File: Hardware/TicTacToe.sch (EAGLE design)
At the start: 42 parts

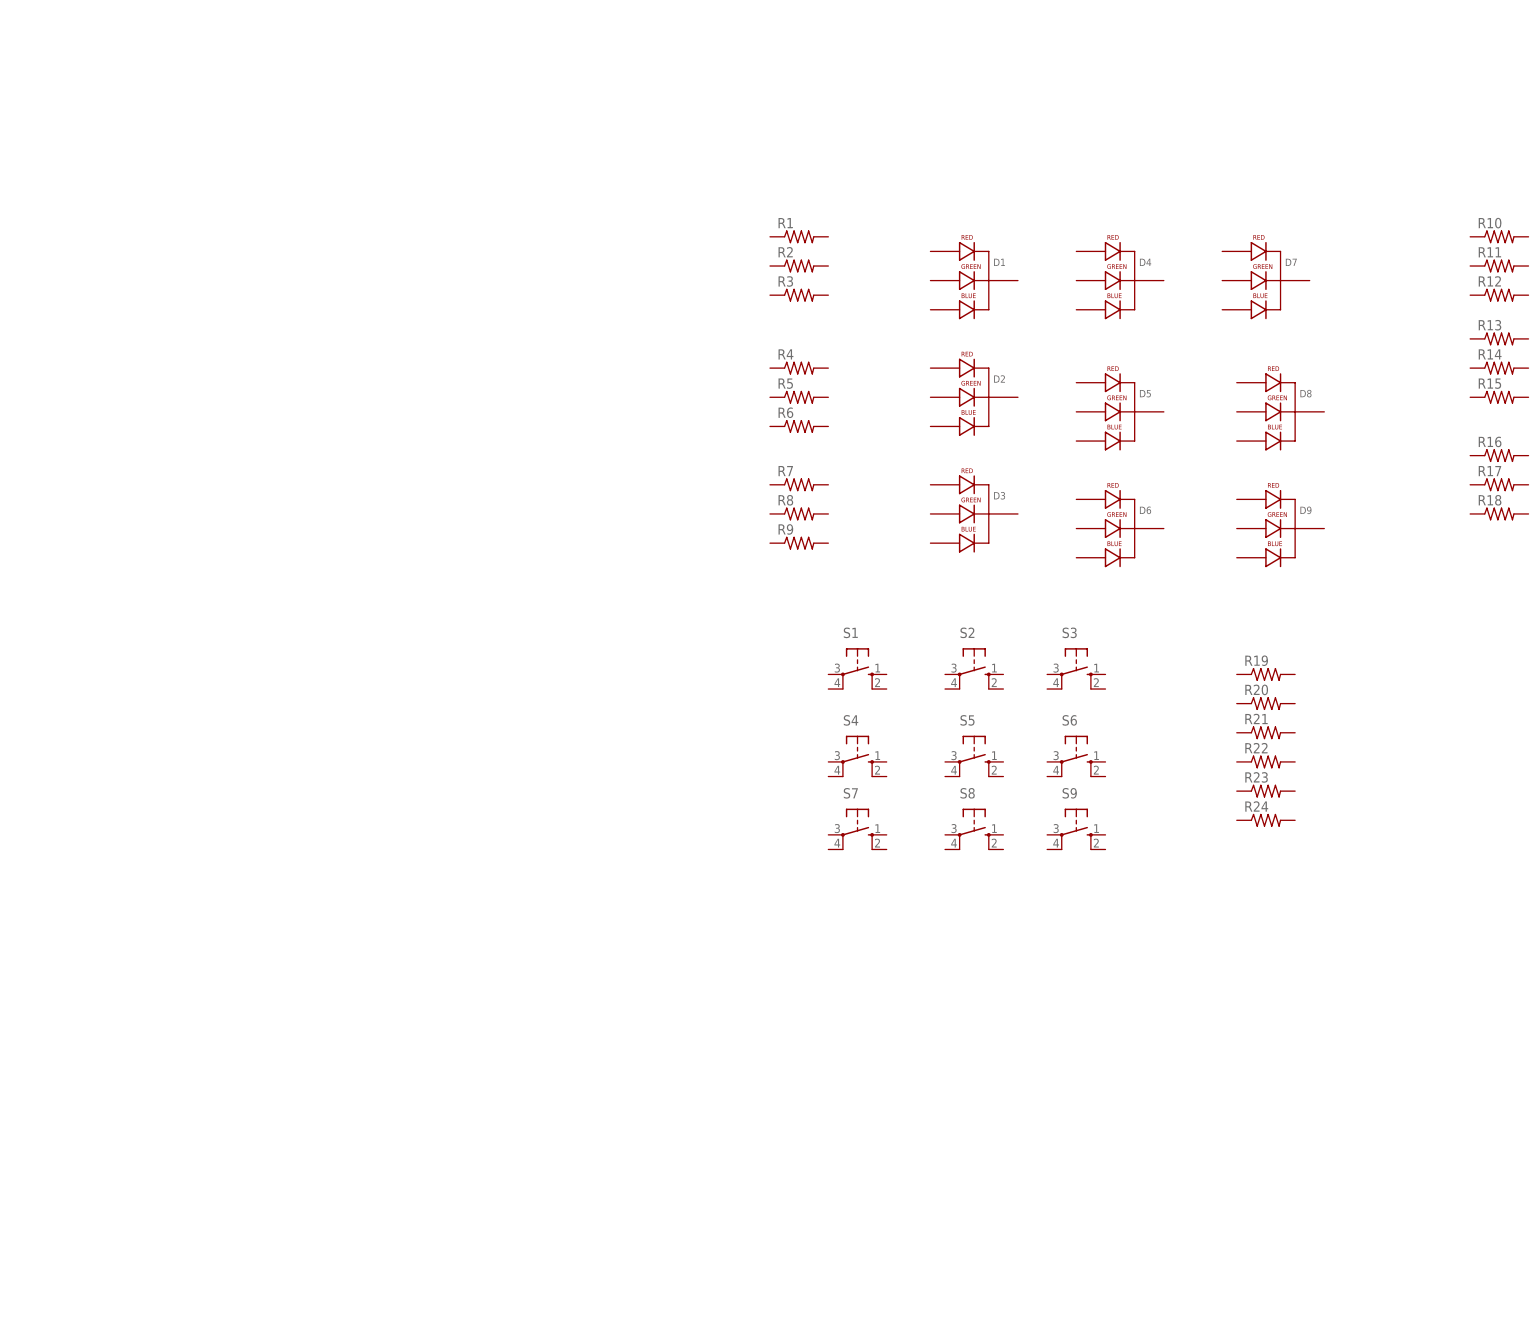
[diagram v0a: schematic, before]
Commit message: Finalizacion del esquematico y montaje del pcb board, solo falta enrutado y una revision final
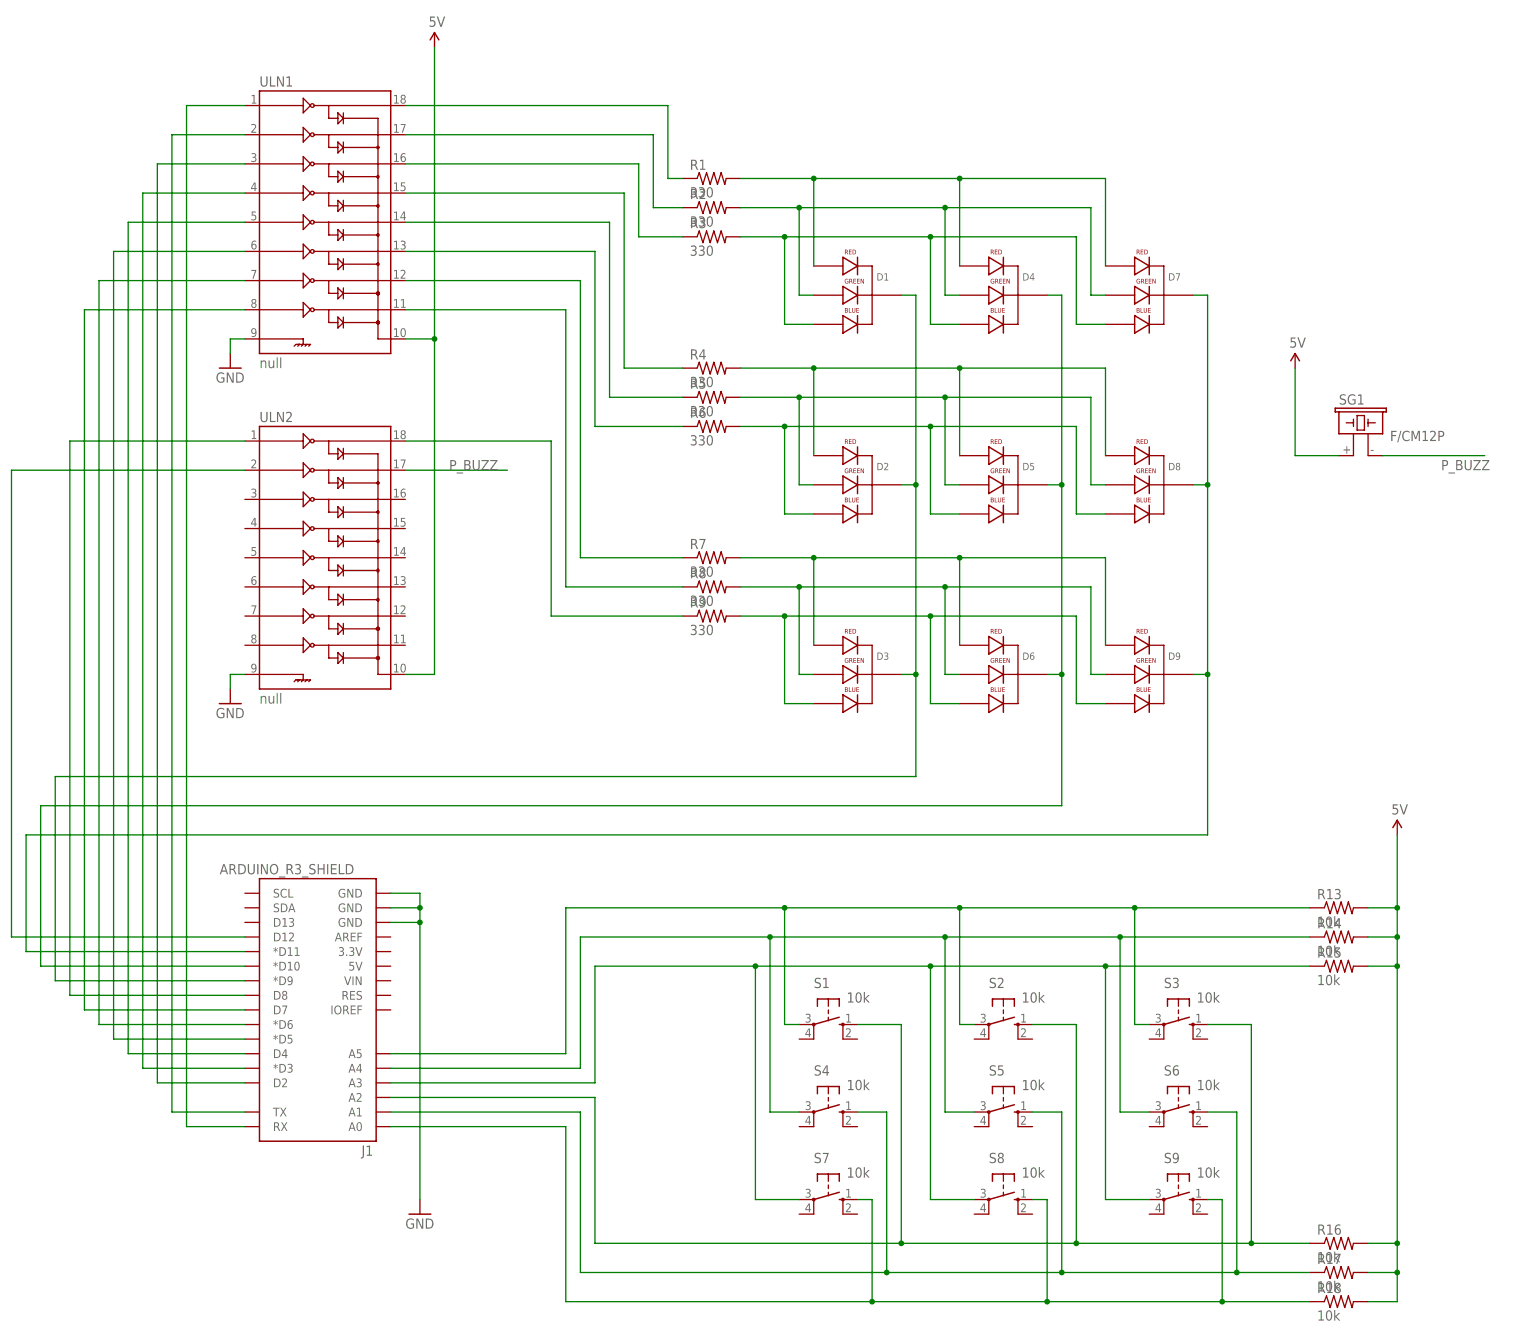
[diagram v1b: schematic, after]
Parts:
- removed R10, R11, R12, R19, R20, R21, R22, R23, R24: (no value), rcl:R-US_0204/7
- added J1: ARDUINO_R3_SHIELD, SparkFun-Boards:ARDUINO_R3_SHIELD
- added SG1: F/CM12P, buzzer:F/CM12P
- added ULN1, ULN2: null, SparkFun-PowerIC:ULN2803DIP
- R1, R2, R3, R4, R5, R6, R7, R8, R9: value (none) -> 330
- R13, R14, R15, R16, R17, R18, S1, S2, S3, S4, S5, S6, S7, S8, S9: value (none) -> 10k
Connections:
- new net 5V: R13.2, R14.2, R15.2, R16.2, R17.2, R18.2, SG1.1, ULN1.10, ULN2.10
- new net GND: J1.GND@0, J1.GND@1, J1.GND@2, ULN1.9, ULN2.9
- new net N$1: D1.RED_CATHODE, D4.RED_CATHODE, D7.RED_CATHODE, R1.2
- new net N$13: J1.A5, R13.1, S1.P, S2.P, S3.P
- new net N$18: J1.A0, R18.1, S7.S, S8.S, S9.S
- new net N$19: R1.1, ULN1.18
- new net N$2: D1.GREEN_CATHODE, D4.GREEN_CATHODE, D7.GREEN_CATHODE, R2.2
- new net N$20: R2.1, ULN1.17
- new net N$21: R3.1, ULN1.16
- new net N$22: R4.1, ULN1.15
- new net N$23: R5.1, ULN1.14
- new net N$24: R6.1, ULN1.13
- new net N$25: R7.1, ULN1.12
- new net N$26: R8.1, ULN1.11
- new net N$27: R9.1, ULN2.18
- new net N$28: J1.RX, ULN1.1
- new net N$29: J1.TX, ULN1.2
- new net N$3: D1.BLUE_CATHODE, D4.BLUE_CATHODE, D7.BLUE_CATHODE, R3.2
- new net N$30: J1.D8, ULN2.1
- new net N$31: J1.D2, ULN1.3
- new net N$32: J1.*D3, ULN1.4
- new net N$33: J1.D4, ULN1.5
- new net N$34: J1.*D5, ULN1.6
- new net N$35: J1.*D6, ULN1.7
- new net N$36: J1.D7, ULN1.8
- new net N$37: D1.CATHODE, D2.CATHODE, D3.CATHODE, J1.*D9
- new net N$4: D2.BLUE_CATHODE, D5.BLUE_CATHODE, D8.BLUE_CATHODE, R6.2
- new net N$41: J1.D12, ULN2.2
- new net N$42: D4.CATHODE, D5.CATHODE, D6.CATHODE, J1.*D10
- new net N$43: D7.CATHODE, D8.CATHODE, D9.CATHODE, J1.*D11
- new net N$44: J1.A1, R17.1, S4.S, S5.S, S6.S
- new net N$45: J1.A2, R16.1, S1.S, S2.S, S3.S
- new net N$46: J1.A3, R15.1, S7.P, S8.P, S9.P
- new net N$47: J1.A4, R14.1, S4.P, S5.P, S6.P
- new net N$5: D2.RED_CATHODE, D5.RED_CATHODE, D8.RED_CATHODE, R4.2
- new net N$6: D2.GREEN_CATHODE, D5.GREEN_CATHODE, D8.GREEN_CATHODE, R5.2
- new net N$7: D3.RED_CATHODE, D6.RED_CATHODE, D9.RED_CATHODE, R7.2
- new net N$8: D3.GREEN_CATHODE, D6.GREEN_CATHODE, D9.GREEN_CATHODE, R8.2
- new net N$9: D3.BLUE_CATHODE, D6.BLUE_CATHODE, D9.BLUE_CATHODE, R9.2
- new net P_BUZZ: SG1.2, ULN2.17
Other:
- moved on the sheet: D1, D2, D3, D4, D5, D6, D7, D8, D9, R1, R13, R14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

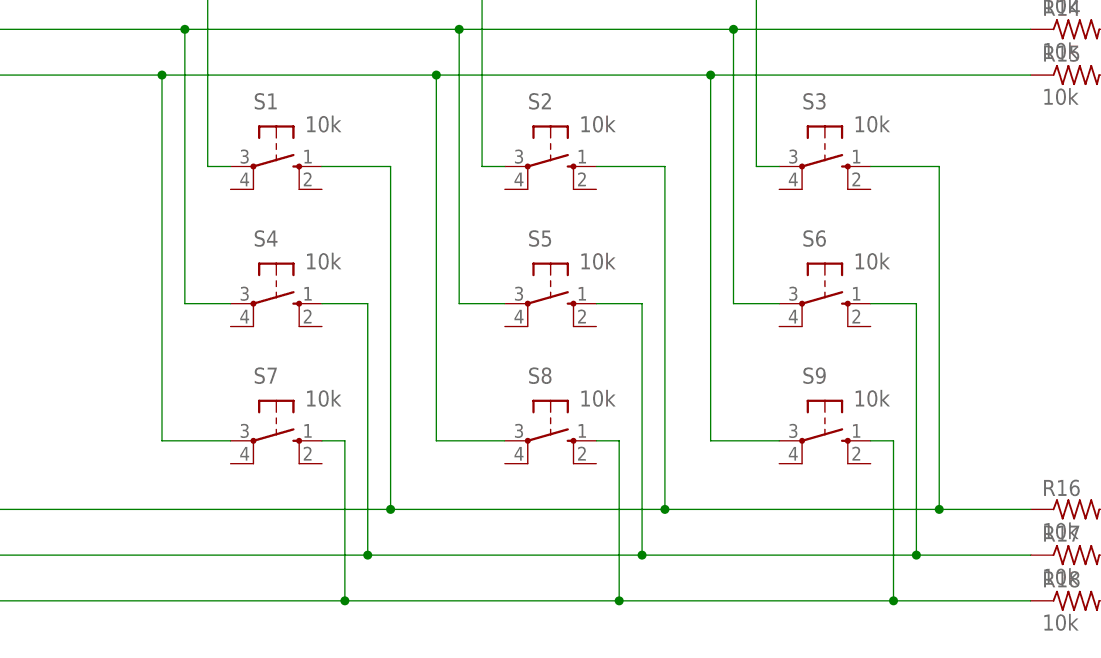
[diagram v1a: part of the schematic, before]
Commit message: Pequeño enrutado del pcb board
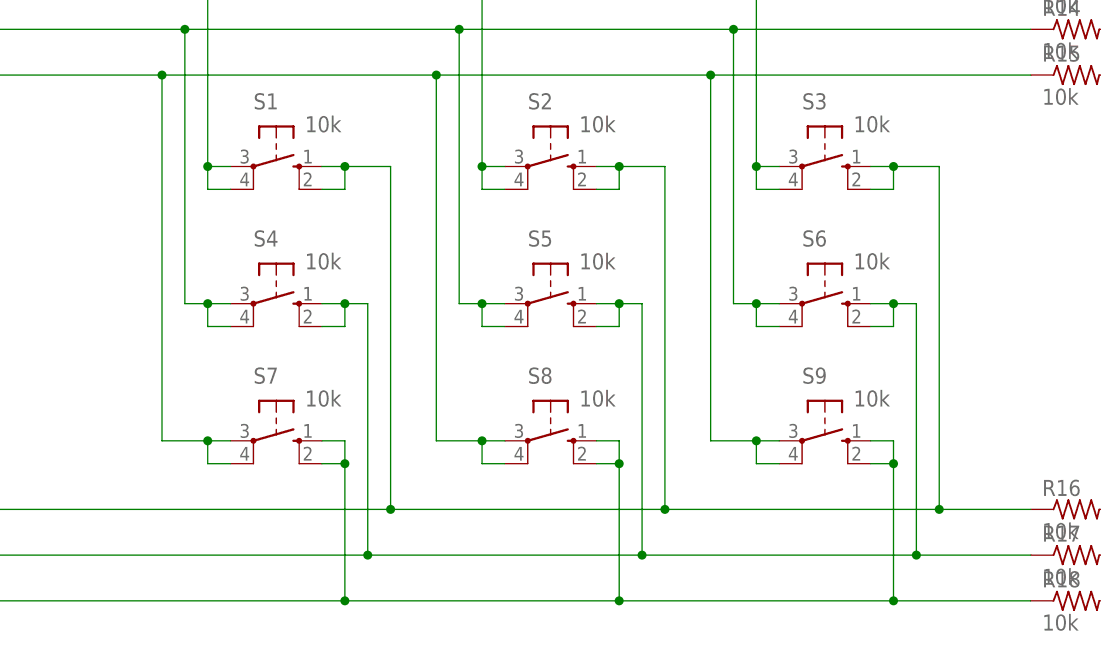
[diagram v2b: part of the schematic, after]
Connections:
- net N$13: now also S1.P1, S2.P1, S3.P1
- net N$18: now also S7.S1, S8.S1, S9.S1
- net N$44: now also S4.S1, S5.S1, S6.S1
- net N$45: now also S1.S1, S2.S1, S3.S1
- net N$46: now also S7.P1, S8.P1, S9.P1
- net N$47: now also S4.P1, S5.P1, S6.P1
